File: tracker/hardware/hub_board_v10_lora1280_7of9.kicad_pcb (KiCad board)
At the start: 4 copper layers, 72 x 80 mm, 49 parts, among them U1 U1, U2 U2, U3 U3, U5 U5, U6 U6, U7 U7

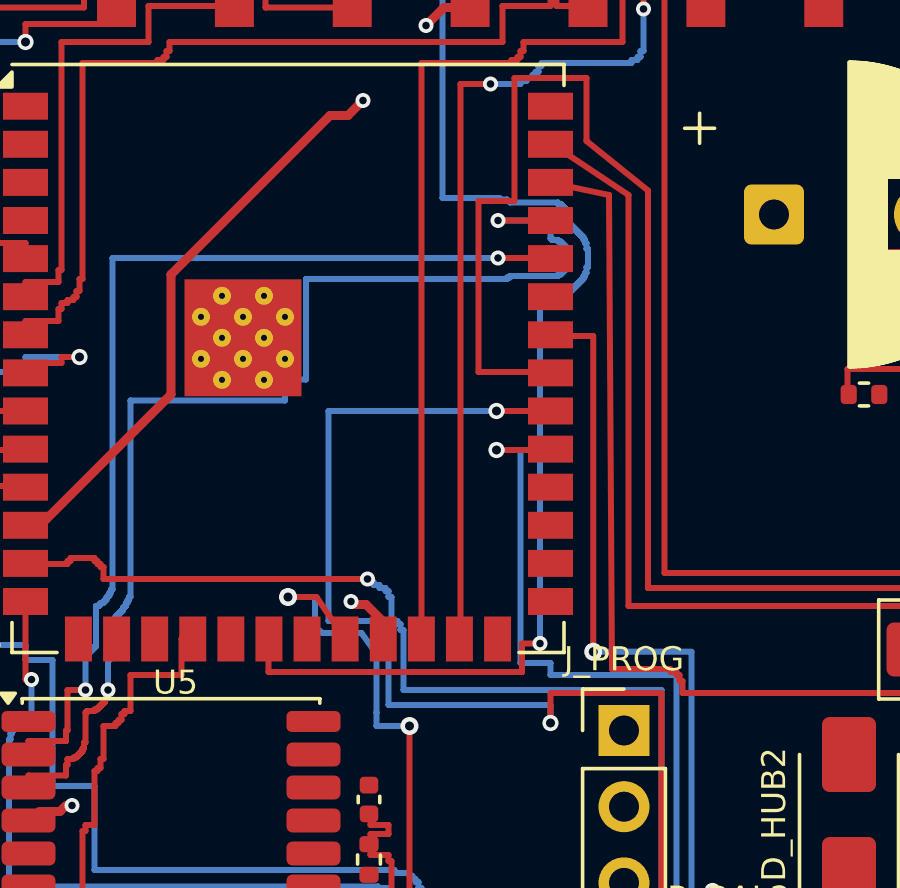
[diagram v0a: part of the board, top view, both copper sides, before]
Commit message: route(hub): operator clears the last 5 violations -- LoRa1280 interface now 9/9 with clearance 0
His nudge commit 7129c584 on c03rad0r/balloon-fresh-1, graded here at the ORIGINAL rules
(0.20 clearance / 0.20 track / 0.50 via / 0.30 drill). Nothing relaxed, nothing shrunk.

RESULT
  total violations        74   (baseline 74 -- exactly back to where it was before routing)
  clearance                0   <- was 5
  shorting_items           0
  solder_mask_bridge       0
  unrouted LoRa1280 nets   0   <- the ADR-140 D3 gate
  unconnected items       86   (unchanged; the rest of the hub)

The five he cleared, all confirmed gone:
  V1/V2 /I2C_SDA vs /I2C_SCL F.Cu            0.1606 -> clear
  V3/V4 /SPI1_SCK vs /E28_RESET_N B.Cu       0.1487 -> clear
  V5    Pad21 /F33_VSENSE (U1) vs /SPI1_SCK   0.1533 -> clear

A CORRESPONDENCE ERROR OF MINE, corrected in this commit. The first check I ran said
"/SPI1_SCK, /SPI1_MOSI, /SPI1_MISO unconnected". Both the DRC and my check were right; my
QUESTION was wrong. Those three nets also run to U3 and U_C (the LR2021 radios), which are
still unrouted, so their names legitimately appear in the unconnected list while the module
end is perfect. The correct test is whether an unconnected item names a PAD OF U_LORA1280 --
that returns 3 items, and all three are power/ground plane joins (Pad 3 +3V3 to U6 and to
J_PROG, Pad 14 GND to the GND_FCu zone), not the interface. All 9 interface nets are
connected AT THE MODULE. This is the second time this session that a net-name match gave a
false answer; the pad-uuid test is the one that holds.

He also rerouted /USB_DN (21 tracks out, 6 in) and /I2C_SCL (15 out, 16 in) beyond the five
sites. Graded because an accidentally-deleted stub is invisible in a violation count: both
USB nets still have their pads, segments and a via (USB_DN 19 segs F.Cu/B.Cu, USB_DP 46 segs),
and neither appears in the unconnected list. The rerouting is sound.

Board committed REFILLED (Edit > Fill All Zones before DRC). H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
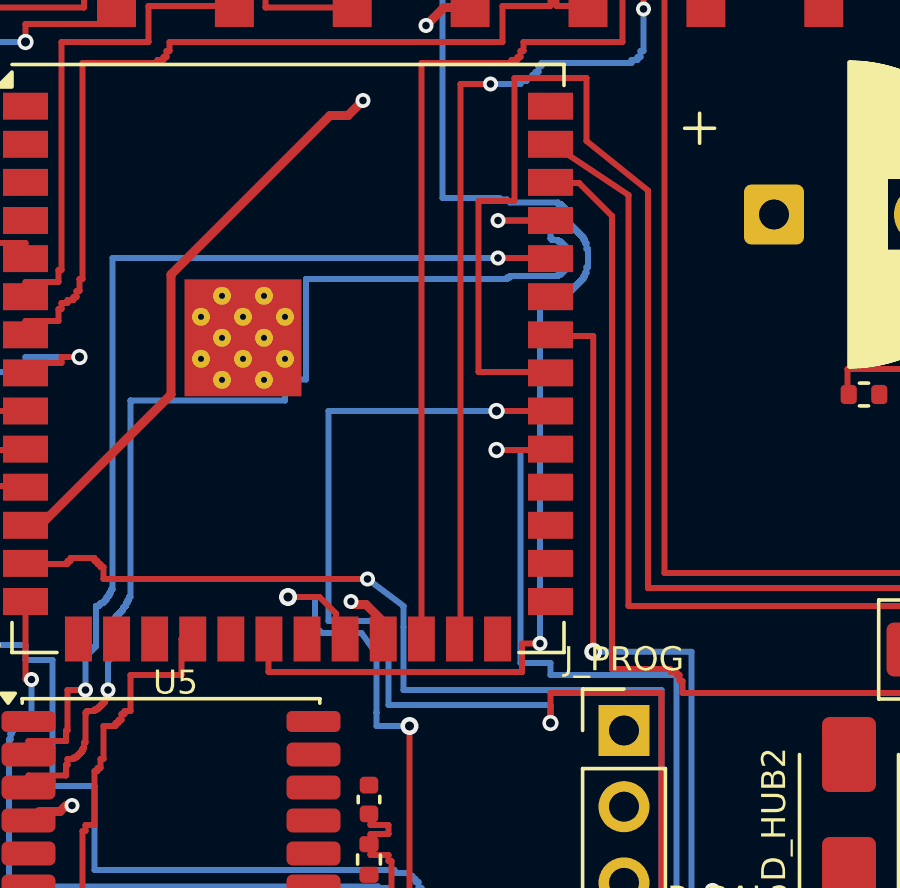
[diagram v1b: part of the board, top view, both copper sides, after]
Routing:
- net /USB_DN: track 36.1 -> 33.4 mm
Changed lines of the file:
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@@
 		)
 	)
+	(gr_line
+		(start 23.65 50.55)
+		(end 22.45 49.65)
+		(stroke
+			(width 0.2)
+			(type default)
+		)
+		(layer "B.Cu")
+		(net 47)
+	)
+	(gr_line
+		(start 23.65 51.25)
+		(end 23.65 50.55)
+		(stroke
+			(width 0.2)
+			(type default)
+		)
+		(layer "B.Cu")
+		(net 47)
+	)
 	(gr_rect
 		(start 0 0)
@@
 	)
 	(segment
-		(start 32.55 52.65)
-		(end 32.55 52.75)
+		(start 54.25 54.95)
+		(end 55.45 54.95)
 		(width 0.2)
 		(layer "F.Cu")
@@
 	)
 	(segment
-		(start 54.25 54.15)
-		(end 54.25 54.95)
+		(start 51.05 53.45)
+		(end 51.05 54.15)
 		(width 0.2)
 		(layer "F.Cu")
@@
 	)
 	(segment
-		(start 51.05 54.15)
-		(end 54.25 54.15)
+		(start 29.5 36.45)
+		(end 30.6 37.55)
 		(width 0.2)
 		(layer "F.Cu")
@@
 	)
 	(segment
-		(start 32.75 52.85)
-		(end 32.85 52.85)
+		(start 32.85 53.05)
+		(end 32.95 53.05)
 		(width 0.2)
 		(layer "F.Cu")
@@
 	)
 	(segment
-		(start 32.75 52.75)
-		(end 32.75 52.85)
+		(start 32.95 53.05)
+		(end 32.95 53.45)
 		(width 0.2)
 		(layer "F.Cu")
@@
 	)
 	(segment
-		(start 32.95 53.05)
-		(end 32.95 53.45)
+		(start 32.55 52.65)
+		(end 32.55 52.75)
 		(width 0.2)
 		(layer "F.Cu")
@@
 	)
 	(segment
-		(start 28.6 36.45)
-		(end 30.5 36.85)
+		(start 30.6 37.55)
+		(end 30.6 52.65)
 		(width 0.2)
 		(layer "F.Cu")
@@
 	)
 	(segment
-		(start 54.25 54.95)
-		(end 55.45 54.95)
+		(start 32.95 53.45)
+		(end 51.05 53.45)
 		(width 0.2)
 		(layer "F.Cu")
@@
 	)
 	(segment
-		(start 32.95 53.45)
-		(end 51.05 53.45)
+		(start 32.75 52.85)
+		(end 32.85 52.85)
 		(width 0.2)
 		(layer "F.Cu")
@@
 	)
 	(segment
-		(start 51.05 53.45)
-		(end 51.05 54.15)
+		(start 32.85 52.85)
+		(end 32.85 53.05)
 		(width 0.2)
 		(layer "F.Cu")
@@
 	)
 	(segment
-		(start 32.85 53.05)
-		(end 32.95 53.05)
+		(start 32.55 52.75)
+		(end 32.75 52.75)
 		(width 0.2)
 		(layer "F.Cu")
@@
 	)
 	(segment
-		(start 30.5 36.85)
-		(end 30.6 52.65)
+		(start 28.6 36.45)
+		(end 29.5 36.45)
 		(width 0.2)
 		(layer "F.Cu")
@@
 	)
 	(segment
-		(start 30.6 52.65)
-		(end 32.55 52.65)
+		(start 54.25 54.15)
+		(end 54.25 54.95)
 		(width 0.2)
 		(layer "F.Cu")
@@
 	)
 	(segment
-		(start 32.85 52.85)
-		(end 32.85 53.05)
+		(start 32.75 52.75)
+		(end 32.75 52.85)
 		(width 0.2)
 		(layer "F.Cu")
@@
 	)
 	(segment
-		(start 32.55 52.75)
-		(end 32.75 52.75)
+		(start 30.6 52.65)
+		(end 32.55 52.65)
+		(width 0.2)
+		(layer "F.Cu")
+		(net 22)
+	)
+	(segment
+		(start 51.05 54.15)
+		(end 54.25 54.15)
 		(width 0.2)
 		(layer "F.Cu")
@@
 	)
 	(segment
-		(start 22.75 51.05)
-		(end 21.15 51.05)
-		(width 0.2)
-		(layer "B.Cu")
-		(net 33)
-	)
-	(segment
 		(start 48.55 64.45)
 		(end 48.55 62.45)
@@
 	)
 	(segment
-		(start 23.15 53.85)
-		(end 23.15 51.85)
-		(width 0.2)
-		(layer "B.Cu")
-		(net 33)
-	)
-	(segment
-		(start 28.55 53.85)
-		(end 23.15 53.85)
+		(start 22.55 51.05)
+		(end 21.15 51.05)
 		(width 0.2)
 		(layer "B.Cu")
@@
 	)
 	(segment
-		(start 23.05 51.85)
-		(end 23.05 51.65)
+		(start 23.15 53.85)
+		(end 23.15 51.65)
 		(width 0.2)
 		(layer "B.Cu")
@@
 	)
 	(segment
-		(start 22.95 51.65)
-		(end 22.95 51.55)
-		(width 0.2)
-		(layer "B.Cu")
-		(net 33)
-	)
-	(segment
 		(start 21.15 44.05)
 		(end 26.75 44.05)
@@
 	)
 	(segment
-		(start 23.05 51.65)
-		(end 22.95 51.65)
+		(start 35.175 62.45)
+		(end 48.55 62.45)
 		(width 0.2)
 		(layer "B.Cu")
@@
 	)
 	(segment
-		(start 22.75 51.55)
-		(end 22.75 51.05)
+		(start 23.15 51.65)
+		(end 22.55 51.05)
 		(width 0.2)
 		(layer "B.Cu")
@@
 	)
 	(segment
-		(start 22.95 51.55)
-		(end 22.75 51.55)
-		(width 0.2)
-		(layer "B.Cu")
-		(net 33)
-	)
-	(segment
-		(start 35.175 62.45)
-		(end 48.55 62.45)
+		(start 28.55 53.85)
+		(end 23.15 53.85)
 		(width 0.2)
 		(layer "B.Cu")
@@
 	)
 	(segment
-		(start 23.15 51.85)
-		(end 23.05 51.85)
+		(start 21.7 51.65)
+		(end 21.4 51.35)
 		(width 0.2)
-		(layer "B.Cu")
-		(net 33)
+		(layer "F.Cu")
+		(net 34)
 	)
 	(segment
-		(start 43.8 73)
-		(end 45.7 73)
+		(start 21.4 51.35)
+		(end 21.4 50.8)
 		(width 0.2)
 		(layer "F.Cu")
@@
 	)
 	(segment
-		(start 20.75 50.25)
-		(end 19.8 50.25)
+		(start 43.8 73)
+		(end 45.7 73)
 		(width 0.2)
 		(layer "F.Cu")
@@
 	)
 	(segment
-		(start 29.15 61.85)
-		(end 29.15 69.15)
+		(start 21.4 50.8)
+		(end 20.85 50.25)
 		(width 0.2)
 		(layer "F.Cu")
@@
 	)
 	(segment
-		(start 21.7 51.65)
-		(end 20.75 50.25)
+		(start 20.85 50.25)
+		(end 19.8 50.25)
+		(width 0.2)
+		(layer "F.Cu")
+		(net 34)
+	)
+	(segment
+		(start 29.15 61.85)
+		(end 29.15 69.15)
 		(width 0.2)
 		(layer "F.Cu")
@@
 	)
 	(segment
-		(start 23.45 51.05)
-		(end 23.45 51.15)
-		(width 0.2)
-		(layer "B.Cu")
-		(net 47)
-	)
-	(segment
-		(start 23.15 50.05)
-		(end 23.15 50.25)
-		(width 0.2)
-		(layer "B.Cu")
-		(net 47)
-	)
-	(segment
-		(start 22.45 49.75)
-		(end 22.65 49.75)
+		(start 30.95 61.05)
+		(end 30.95 62.35)
 		(width 0.2)
 		(layer "B.Cu")
@@
 	)
 	(segment
-		(start 23.65 53.35)
-		(end 32.25 53.35)
+		(start 32.25 61.05)
+		(end 30.95 61.05)
 		(width 0.2)
 		(layer "B.Cu")
@@
 	)
 	(segment
-		(start 22.65 49.85)
-		(end 22.85 49.85)
+		(start 23.65 51.25)
+		(end 23.65 53.35)
 		(width 0.2)
 		(layer "B.Cu")
@@
 	)
 	(segment
-		(start 23.05 49.95)
-		(end 23.05 50.05)
-		(width 0.2)
-		(layer "B.Cu")
-		(net 47)
-	)
-	(segment
-		(start 23.25 51.05)
-		(end 23.45 51.05)
-		(width 0.2)
-		(layer "B.Cu")
-		(net 47)
-	)
-	(segment
-		(start 23.15 50.25)
-		(end 23.25 50.25)
-		(width 0.2)
-		(layer "B.Cu")
-		(net 47)
-	)
-	(segment
-		(start 22.85 49.85)
-		(end 22.85 49.95)
-		(width 0.2)
-		(layer "B.Cu")
-		(net 47)
-	)
-	(segment
-		(start 22.65 49.75)
-		(end 22.65 49.85)
-		(width 0.2)
-		(layer "B.Cu")
-		(net 47)
-	)
-	(segment
 		(start 22.45 49.65)
 		(end 22.45 49.75)
@@
 	)
 	(segment
-		(start 23.65 51.35)
-		(end 23.65 53.35)
-		(width 0.2)
-		(layer "B.Cu")
-		(net 47)
-	)
-	(segment
-		(start 23.55 51.35)
-		(end 23.65 51.35)
-		(width 0.2)
-		(layer "B.Cu")
-		(net 47)
-	)
-	(segment
-		(start 23.25 50.25)
-		(end 23.25 51.05)
-		(width 0.2)
-		(layer "B.Cu")
-		(net 47)
-	)
-	(segment
-		(start 23.05 50.05)
-		(end 23.15 50.05)
-		(width 0.2)
-		(layer "B.Cu")
-		(net 47)
-	)
-	(segment
-		(start 23.45 51.15)
-		(end 23.55 51.15)
-		(width 0.2)
-		(layer "B.Cu")
-		(net 47)
-	)
-	(segment
-		(start 32.25 61.05)
-		(end 30.95 61.05)
-		(width 0.2)
-		(layer "B.Cu")
-		(net 47)
-	)
-	(segment
-		(start 22.85 49.95)
-		(end 23.05 49.95)
-		(width 0.2)
-		(layer "B.Cu")
-		(net 47)
-	)
-	(segment
-		(start 23.55 51.15)
-		(end 23.55 51.35)
-		(width 0.2)
-		(layer "B.Cu")
-		(net 47)
-	)
-	(segment
-		(start 30.95 61.05)
-		(end 30.95 62.35)
+		(start 23.65 53.35)
+		(end 32.25 53.35)
 		(width 0.2)
 		(layer "B.Cu")
